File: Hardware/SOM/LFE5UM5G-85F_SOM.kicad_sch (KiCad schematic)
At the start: 0 parts

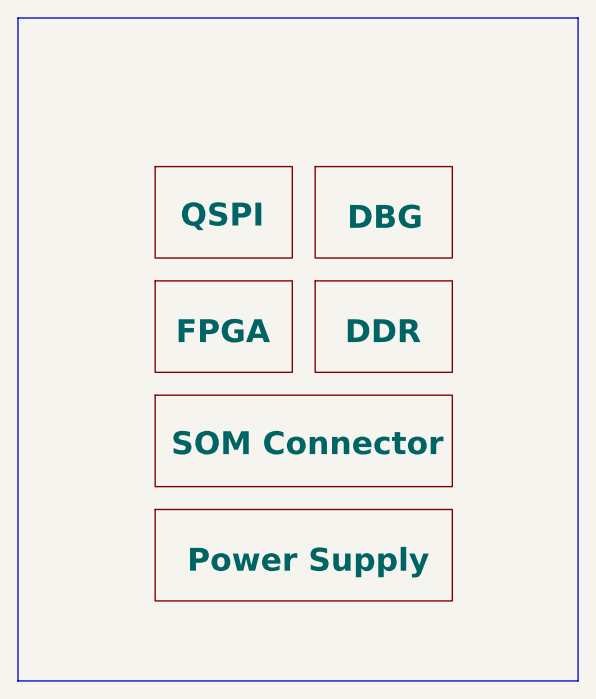
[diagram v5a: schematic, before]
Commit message: PCIe AC coupling
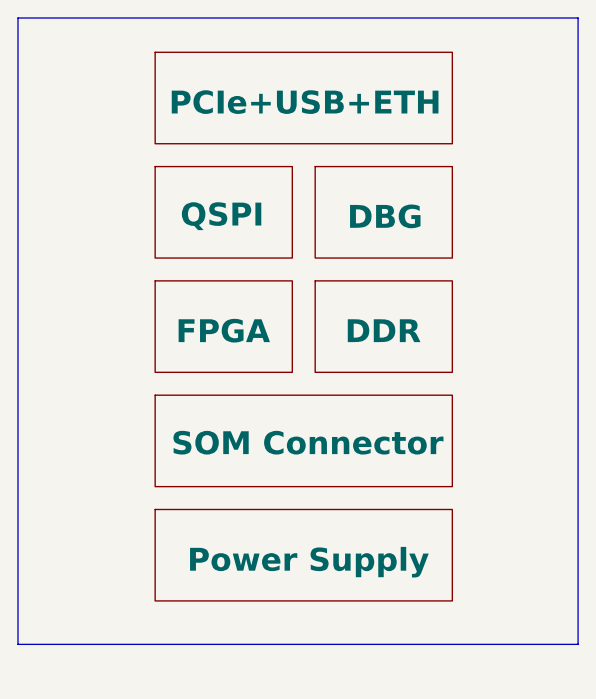
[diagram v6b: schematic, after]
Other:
- added sheet PCIe+USB+ETH (Interfaces.kicad_sch)
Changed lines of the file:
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@@
 	(rectangle
 		(start 72.39 81.28)
-		(end 134.62 154.94)
+		(end 134.62 150.876)
 		(stroke
 			(width 0)
@@
 				)
 			)
+		)
+	)
+	(sheet
+		(at 87.63 85.09)
+		(size 33.02 10.16)
+		(exclude_from_sim no)
+		(in_bom yes)
+		(on_board yes)
+		(dnp no)
+		(stroke
+			(width 0.1524)
+			(type solid)
+		)
+		(fill
+			(color 0 0 0 0.0000)
+		)
+		(property "Sheetname" "PCIe+USB+ETH"
+			(at 89.154 92.202 0)
+			(effects
+				(font
+					(size 2.54 2.54)
+					(thickness 0.508)
+					(bold yes)
+				)
+				(justify left bottom)
+			)
+		)
+		(property "Sheetfile" "Interfaces.kicad_sch"
+			(at 87.63 95.8346 0)
+			(effects
+				(font
+					(size 1.27 1.27)
+				)
+				(justify left top)
+				(hide yes)
+			)
+		)
+		(instances
+			(project "LFE5UM5G-85F_SOM"
+				(path "/de32abb0-ff3b-4c67-a91a-eed08140b1b2"
+					(page "8")
+				)
+			)

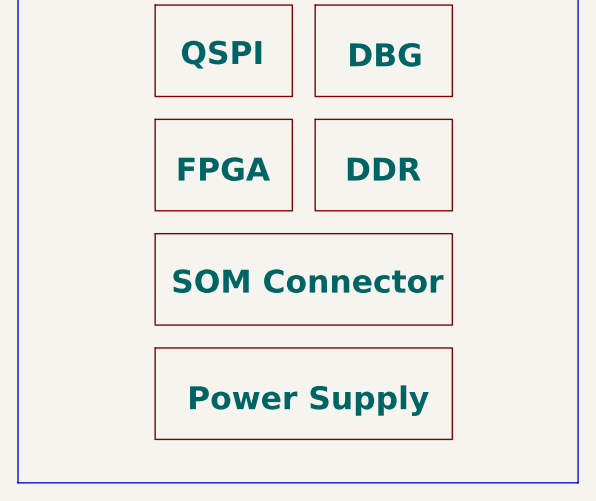
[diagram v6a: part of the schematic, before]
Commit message: SOM: decoupling caps placement
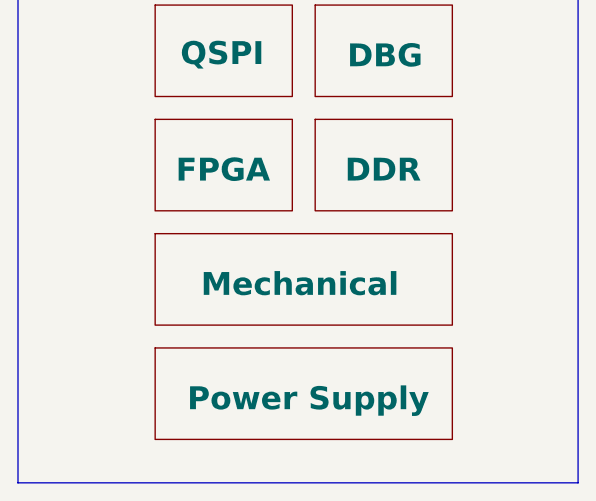
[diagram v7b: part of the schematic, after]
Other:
- sheet SOM Connector renamed Mechanical
- sheet Mechanical: file Connector.kicad_sch -> Mechanical.kicad_sch
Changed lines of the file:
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@@
 			(color 0 0 0 0.0000)
 		)
-		(property "Sheetname" "SOM Connector"
-			(at 89.408 130.048 0)
+		(property "Sheetname" "Mechanical"
+			(at 92.71 130.302 0)
 			(effects
 				(font
@@
 			)
 		)
-		(property "Sheetfile" "Connector.kicad_sch"
+		(property "Sheetfile" "Mechanical.kicad_sch"
 			(at 87.63 133.9346 0)
 			(effects
